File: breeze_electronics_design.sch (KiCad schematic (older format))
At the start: 100 parts, among them U1 STM32F103T8U6TR

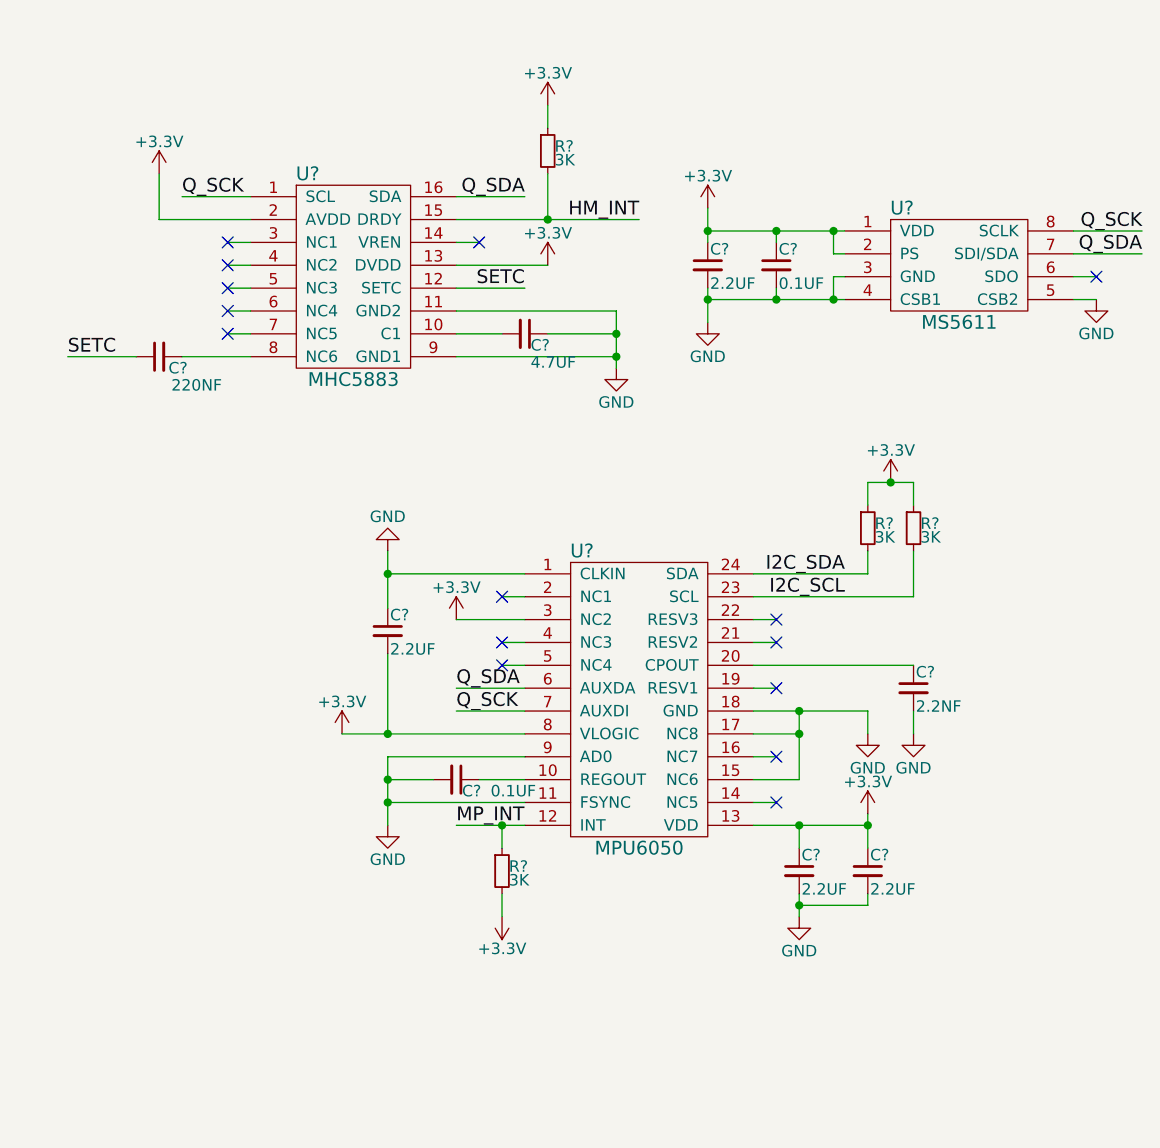
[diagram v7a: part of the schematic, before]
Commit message: Modify the schematic of sensor
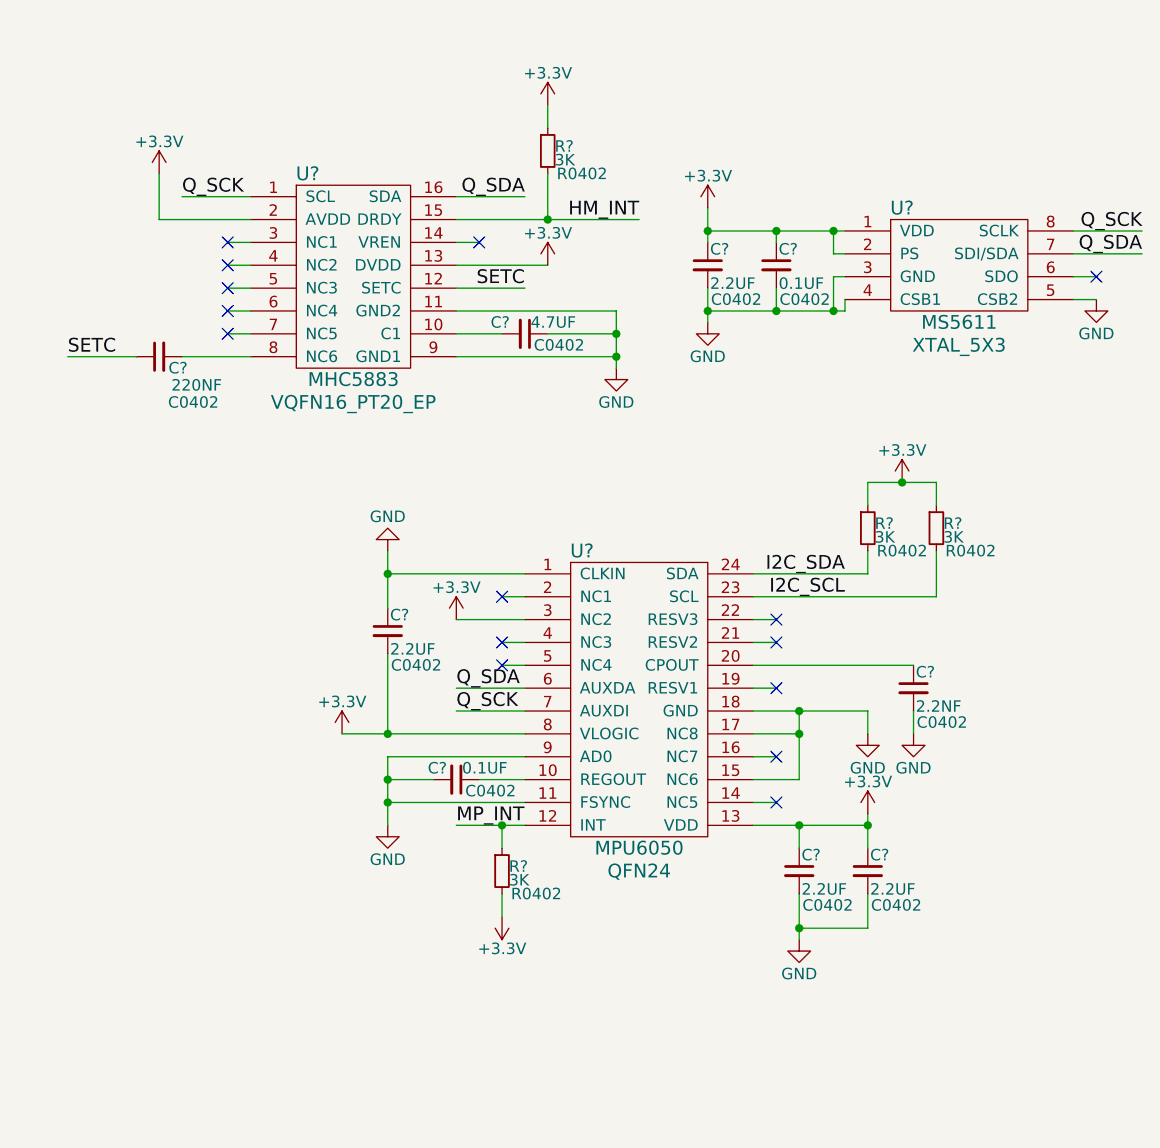
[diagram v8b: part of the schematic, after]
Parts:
- C? (x9): footprint (none) -> C0402
- R? (x4): footprint (none) -> R0402
- U?: footprint (none) -> VQFN16_PT20_EP
- U?: footprint (none) -> XTAL_5X3
- U?: footprint (none) -> QFN24
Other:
- moved on the sheet: R?
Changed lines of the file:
@@
 F 0 "U?" H 12150 5950 60  0000 C CNN
 F 1 "MHC5883" H 12350 5050 60  0000 C CNN
-F 2 "" H 12300 5700 60  0000 C CNN
+F 2 "VQFN16_PT20_EP" H 12350 4950 60  0000 C CNN
 F 3 "" H 12300 5700 60  0000 C CNN
 	1    12350 5500
@@
 F 0 "C?" V 11450 5725 50  0000 L CNN
 F 1 "220NF" V 11375 5575 50  0000 L CNN
-F 2 "" H 11500 5850 50  0000 C CNN
+F 2 "C0402" V 11300 5700 50  0000 C CNN
 F 3 "" H 11500 5850 50  0000 C CNN
 	1    11500 5850
@@
 F 0 "R?" H 13230 4970 50  0000 L CNN
 F 1 "3K" H 13230 4910 50  0000 L CNN
-F 2 "" H 13200 4950 50  0000 C CNN
+F 2 "R0402" H 13350 4850 50  0000 C CNN
 F 3 "" H 13200 4950 50  0000 C CNN
 	1    13200 4950
@@
 U 1 1 57B61D7A
 P 13100 5750
-F 0 "C?" V 13150 5775 50  0000 L CNN
-F 1 "4.7UF" V 13225 5775 50  0000 L CNN
-F 2 "" H 13100 5750 50  0000 C CNN
+F 0 "C?" V 13050 5600 50  0000 L CNN
+F 1 "4.7UF" V 13050 5775 50  0000 L CNN
+F 2 "C0402" V 13150 5900 50  0000 C CNN
 F 3 "" H 13100 5750 50  0000 C CNN
 	1    13100 5750
@@
 F 0 "U?" H 14750 5700 60  0000 C CNN
 F 1 "MS5611" H 15000 5200 60  0000 C CNN
-F 2 "" H 14950 5500 60  0000 C CNN
+F 2 "XTAL_5X3" H 15000 5100 60  0000 C CNN
 F 3 "" H 14950 5500 60  0000 C CNN
 	1    15000 5450
@@
 F 0 "C?" H 13910 5520 50  0000 L CNN
 F 1 "2.2UF" H 13910 5370 50  0000 L CNN
-F 2 "" H 13900 5450 50  0000 C CNN
+F 2 "C0402" H 14025 5300 50  0000 C CNN
 F 3 "" H 13900 5450 50  0000 C CNN
 	1    13900 5450
@@
 F 0 "C?" H 14210 5520 50  0000 L CNN
 F 1 "0.1UF" H 14210 5370 50  0000 L CNN
-F 2 "" H 14200 5450 50  0000 C CNN
+F 2 "C0402" H 14325 5300 50  0000 C CNN
 F 3 "" H 14200 5450 50  0000 C CNN
 	1    14200 5450
@@
 F 0 "U?" H 13350 8000 60  0000 C CNN
 F 1 "MPU6050" H 13600 6700 60  0000 C CNN
-F 2 "" H 13600 7550 60  0000 C CNN
+F 2 "QFN24" H 13600 6600 60  0000 C CNN
 F 3 "" H 13600 7550 60  0000 C CNN
 	1    13600 7350
@@
 F 0 "C?" H 12510 7120 50  0000 L CNN
 F 1 "2.2UF" H 12510 6970 50  0000 L CNN
-F 2 "" H 12500 7050 50  0000 C CNN
+F 2 "C0402" H 12625 6900 50  0000 C CNN
 F 3 "" H 12500 7050 50  0000 C CNN
 	1    12500 7050
@@
 U 1 1 57B6D377
 P 12800 7700
-F 0 "C?" V 12850 7725 50  0000 L CNN
-F 1 "0.1UF" V 12850 7850 50  0000 L CNN
-F 2 "" H 12800 7700 50  0000 C CNN
+F 0 "C?" V 12750 7575 50  0000 L CNN
+F 1 "0.1UF" V 12750 7725 50  0000 L CNN
+F 2 "C0402" V 12850 7850 50  0000 C CNN
 F 3 "" H 12800 7700 50  0000 C CNN
 	1    12800 7700
@@
 F 0 "R?" H 13030 8120 50  0000 L CNN
 F 1 "3K" H 13030 8060 50  0000 L CNN
-F 2 "" H 13000 8100 50  0000 C CNN
+F 2 "R0402" H 13150 8000 50  0000 C CNN
 F 3 "" H 13000 8100 50  0000 C CNN
 	1    13000 8100
@@
 F 0 "R?" H 14630 6620 50  0000 L CNN
 F 1 "3K" H 14630 6560 50  0000 L CNN
-F 2 "" H 14600 6600 50  0000 C CNN
+F 2 "R0402" H 14750 6500 50  0000 C CNN
 F 3 "" H 14600 6600 50  0000 C CNN
 	1    14600 6600
@@
 $EndComp
 $Comp
-L Resistor R?
-U 1 1 57B70D8A
-P 14800 6600
-F 0 "R?" H 14830 6620 50  0000 L CNN
-F 1 "3K" H 14830 6560 50  0000 L CNN
-F 2 "" H 14800 6600 50  0000 C CNN
-F 3 "" H 14800 6600 50  0000 C CNN
-	1    14800 6600
-	1    0    0    -1
-$EndComp
-$Comp
 L +3.3V #PWR?
 U 1 1 57B714A6
-P 14700 6400
-F 0 "#PWR?" H 14700 6250 50  0001 C CNN
-F 1 "+3.3V" H 14700 6540 50  0000 C CNN
-F 2 "" H 14700 6400 50  0000 C CNN
-F 3 "" H 14700 6400 50  0000 C CNN
-	1    14700 6400
+P 14750 6400
+F 0 "#PWR?" H 14750 6250 50  0001 C CNN
+F 1 "+3.3V" H 14750 6540 50  0000 C CNN
+F 2 "" H 14750 6400 50  0000 C CNN
+F 3 "" H 14750 6400 50  0000 C CNN
+	1    14750 6400
 	1    0    0    -1
 $EndComp
@@
 F 0 "C?" H 14810 7370 50  0000 L CNN
 F 1 "2.2NF" H 14810 7220 50  0000 L CNN
-F 2 "" H 14800 7300 50  0000 C CNN
+F 2 "C0402" H 14925 7150 50  0000 C CNN
 F 3 "" H 14800 7300 50  0000 C CNN
 	1    14800 7300
@@
 F 0 "C?" H 14310 8170 50  0000 L CNN
 F 1 "2.2UF" H 14310 8020 50  0000 L CNN
-F 2 "" H 14300 8100 50  0000 C CNN
+F 2 "C0402" H 14425 7950 50  0000 C CNN
 F 3 "" H 14300 8100 50  0000 C CNN
 	1    14300 8100
@@
 F 0 "C?" H 14610 8170 50  0000 L CNN
 F 1 "2.2UF" H 14610 8020 50  0000 L CNN
-F 2 "" H 14600 8100 50  0000 C CNN
+F 2 "C0402" H 14725 7950 50  0000 C CNN
 F 3 "" H 14600 8100 50  0000 C CNN
 	1    14600 8100
@@
 L GND #PWR?
 U 1 1 57B73D7F
-P 14300 8300
-F 0 "#PWR?" H 14300 8050 50  0001 C CNN
-F 1 "GND" H 14300 8150 50  0000 C CNN
-F 2 "" H 14300 8300 50  0000 C CNN
-F 3 "" H 14300 8300 50  0000 C CNN
-	1    14300 8300
+P 14300 8400
+F 0 "#PWR?" H 14300 8150 50  0001 C CNN
+F 1 "GND" H 14300 8250 50  0000 C CNN
+F 2 "" H 14300 8400 50  0000 C CNN
+F 3 "" H 14300 8400 50  0000 C CNN
+	1    14300 8400
 	1    0    0    -1
 $EndComp
@@
 	1    0    0    -1
 $EndComp
+Text Label 2050 4675 0    60   ~ 0
+VBUS
+Text Label 8650 2400 0    60   ~ 0
+SCK
+Text Label 8650 2300 0    60   ~ 0
+CSN
+$Comp
+L +3.3V #PWR?
+U 1 1 57BA0919
+P 9550 1050
+F 0 "#PWR?" H 9550 900 50  0001 C CNN
+F 1 "+3.3V" H 9550 1190 50  0000 C CNN
+F 2 "" H 9550 1050 50  0000 C CNN
+F 3 "" H 9550 1050 50  0000 C CNN
+	1    9550 1050
+	1    0    0    -1
+$EndComp
+$Comp
+L Capacitance C?
+U 1 1 57BAF0AE
+P 12150 2000
+F 0 "C?" H 12160 2070 50  0000 L CNN
+F 1 "0.1UF" H 12150 1925 50  0000 L CNN
+F 2 "C0402" H 12275 1850 50  0000 C CNN
+F 3 "" H 12150 2000 50  0000 C CNN
+	1    12150 2000
+	1    0    0    -1
+$EndComp
+$Comp
+L Capacitance C?
+U 1 1 57BAF0B5
+P 12550 2000
+F 0 "C?" H 12560 2070 50  0000 L CNN
+F 1 "2.2UF" H 12550 1925 50  0000 L CNN
+F 2 "C0402" H 12675 1850 50  0000 C CNN
+F 3 "" H 12550 2000 50  0000 C CNN
+	1    12550 2000
+	1    0    0    -1
+$EndComp
+$Comp
+L GND #PWR?
+U 1 1 57BAF0BC
+P 12350 2300
+F 0 "#PWR?" H 12350 2050 50  0001 C CNN
+F 1 "GND" H 12350 2150 50  0000 C CNN
+F 2 "" H 12350 2300 50  0000 C CNN
+F 3 "" H 12350 2300 50  0000 C CNN
+	1    12350 2300
+	1    0    0    -1
+$EndComp
+$Comp
+L +3.3V #PWR?
+U 1 1 57BAF0C2
+P 12350 1750
+F 0 "#PWR?" H 12350 1600 50  0001 C CNN
+F 1 "+3.3V" H 12350 1890 50  0000 C CNN
+F 2 "" H 12350 1750 50  0000 C CNN
+F 3 "" H 12350 1750 50  0000 C CNN
+	1    12350 1750
+	1    0    0    -1
+$EndComp
 Wire Wire Line
 	3550 2800 3550 3100
@@
 Connection ~ 13900 5300
 Wire Wire Line
-	14200 5550 14200 5600
-Wire Wire Line
-	13900 5600 14500 5600
-Connection ~ 13900 5600
-Connection ~ 14200 5600
-Wire Wire Line
-	13900 5550 13900 5700
-Wire Wire Line
 	14200 5350 14200 5300
 Connection ~ 14200 5300
@@
 Connection ~ 14450 5300
 Wire Wire Line
-	14500 5500 14450 5500
-Wire Wire Line
-	14450 5500 14450 5600
-Connection ~ 14450 5600
-Wire Wire Line
 	15600 5500 15500 5500
 Wire Wire Line
@@
 	14100 6800 14600 6800
 Wire Wire Line
-	14100 6900 14800 6900
+	14100 6900 14900 6900
 Wire Wire Line
 	14600 6800 14600 6700
-Wire Wire Line
-	14800 6900 14800 6700
-Wire Wire Line
-	14600 6400 14800 6400
-Wire Wire Line
-	14600 6400 14600 6500
-Wire Wire Line
-	14800 6400 14800 6500
-Connection ~ 14700 6400
 Wire Wire Line
 	14800 7500 14800 7400
@@
 Connection ~ 14300 7500
 Wire Wire Line
-	14300 8200 14300 8300
-Wire Wire Line
-	14300 8250 14600 8250
-Wire Wire Line
-	14600 8250 14600 8200
-Connection ~ 14300 8250
+	14600 8200 14600 8350
 Wire Wire Line
 	14100 7900 14600 7900
@@
 	4900 4025 4600 4025
 Connection ~ 4600 4025
-Text Label 2050 4675 0    60   ~ 0
-VBUS
 Wire Wire Line
 	8650 2500 8850 2500
 Wire Wire Line
 	8650 2600 8850 2600
-Text Label 8650 2400 0    60   ~ 0
-SCK
 Wire Wire Line
 	8650 2400 8850 2400
-Text Label 8650 2300 0    60   ~ 0
-CSN
 Wire Wire Line
 	8650 2300 8850 2300
 Wire Wire Line
 	8650 2200 8850 2200
-$Comp
-L +3.3V #PWR?
-U 1 1 57BA0919
-P 9550 1050
-F 0 "#PWR?" H 9550 900 50  0001 C CNN
-F 1 "+3.3V" H 9550 1190 50  0000 C CNN
-F 2 "" H 9550 1050 50  0000 C CNN
-F 3 "" H 9550 1050 50  0000 C CNN
-	1    9550 1050
-	1    0    0    -1
-$EndComp
-$Comp
-L Capacitance C?
-U 1 1 57BAF0AE
-P 12150 2000
-F 0 "C?" H 12160 2070 50  0000 L CNN
-F 1 "0.1UF" H 12150 1925 50  0000 L CNN
-F 2 "C0402" H 12275 1850 50  0000 C CNN
-F 3 "" H 12150 2000 50  0000 C CNN
-	1    12150 2000
-	1    0    0    -1
-$EndComp
-$Comp
-L Capacitance C?
-U 1 1 57BAF0B5
-P 12550 2000
-F 0 "C?" H 12560 2070 50  0000 L CNN
-F 1 "2.2UF" H 12550 1925 50  0000 L CNN
-F 2 "C0402" H 12675 1850 50  0000 C CNN
-F 3 "" H 12550 2000 50  0000 C CNN
-	1    12550 2000
-	1    0    0    -1
-$EndComp
-$Comp
-L GND #PWR?
-U 1 1 57BAF0BC
-P 12350 2300
-F 0 "#PWR?" H 12350 2050 50  0001 C CNN
-F 1 "GND" H 12350 2150 50  0000 C CNN
-F 2 "" H 12350 2300 50  0000 C CNN
-F 3 "" H 12350 2300 50  0000 C CNN
-	1    12350 2300
-	1    0    0    -1
-$EndComp
-$Comp
-L +3.3V #PWR?
-U 1 1 57BAF0C2
-P 12350 1750
-F 0 "#PWR?" H 12350 1600 50  0001 C CNN
-F 1 "+3.3V" H 12350 1890 50  0000 C CNN
-F 2 "" H 12350 1750 50  0000 C CNN
-F 3 "" H 12350 1750 50  0000 C CNN
-	1    12350 1750
-	1    0    0    -1
-$EndComp
 Wire Wire Line
 	12150 2100 12150 2200
@@
 	9150 7150 9150 6950
 Connection ~ 8750 7150
+Wire Wire Line
+	13900 5550 13900 5700
+Wire Wire Line
+	13900 5650 14500 5650
+Wire Wire Line
+	14200 5650 14200 5550
+Connection ~ 13900 5650
+Wire Wire Line
+	14500 5650 14500 5600
+Connection ~ 14200 5650
+Wire Wire Line
+	14500 5500 14450 5500
+Wire Wire Line
+	14450 5500 14450 5650
+Connection ~ 14450 5650
+$Comp
+L Resistor R?
+U 1 1 57B70D8A
+P 14900 6600
+F 0 "R?" H 14930 6620 50  0000 L CNN
+F 1 "3K" H 14930 6560 50  0000 L CNN
+F 2 "R0402" H 15050 6500 50  0000 C CNN
+F 3 "" H 14900 6600 50  0000 C CNN
+	1    14900 6600
+	1    0    0    -1
+$EndComp
+Wire Wire Line
+	14900 6900 14900 6700
+Wire Wire Line
+	14600 6500 14600 6400
+Wire Wire Line
+	14600 6400 14900 6400
+Wire Wire Line
+	14900 6400 14900 6500
+Connection ~ 14750 6400
+Wire Wire Line
+	14300 8400 14300 8200
+Wire Wire Line
+	14600 8350 14300 8350
+Connection ~ 14300 8350
 $EndSCHEMATC
